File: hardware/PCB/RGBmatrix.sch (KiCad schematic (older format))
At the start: 41 parts

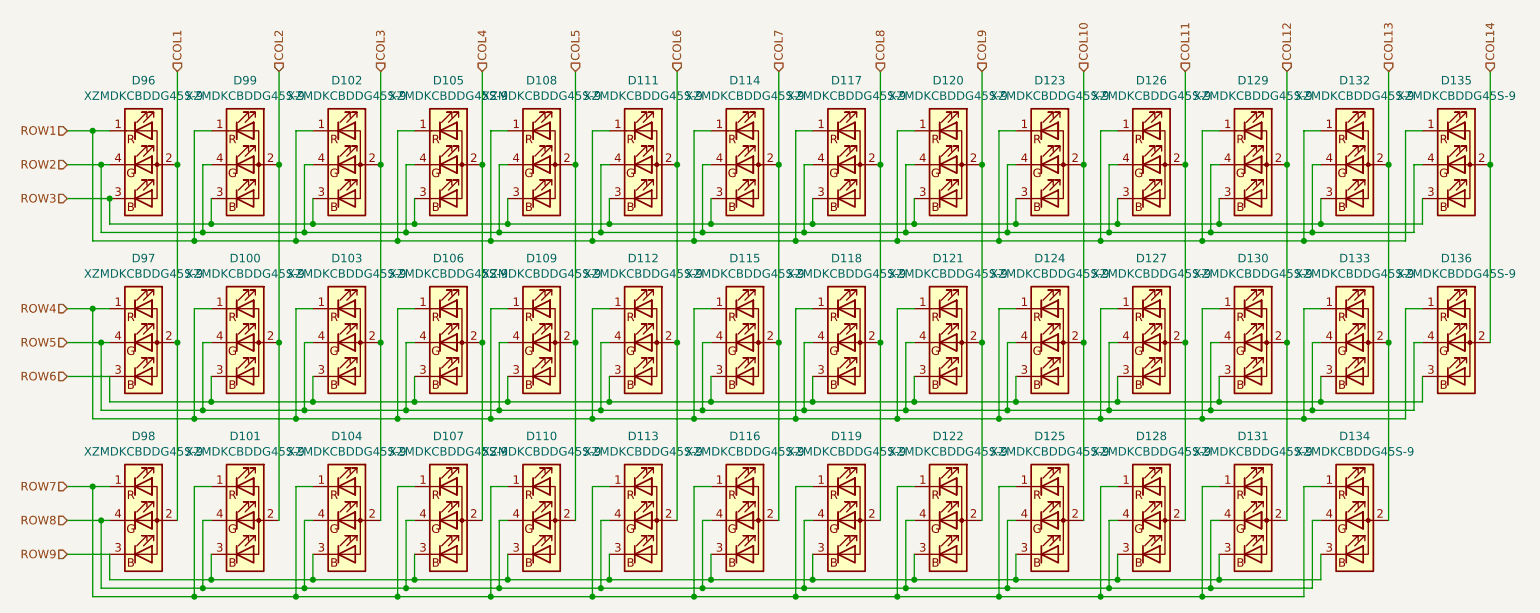
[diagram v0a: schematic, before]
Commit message: update render, remove useless files, fix the decoupeling
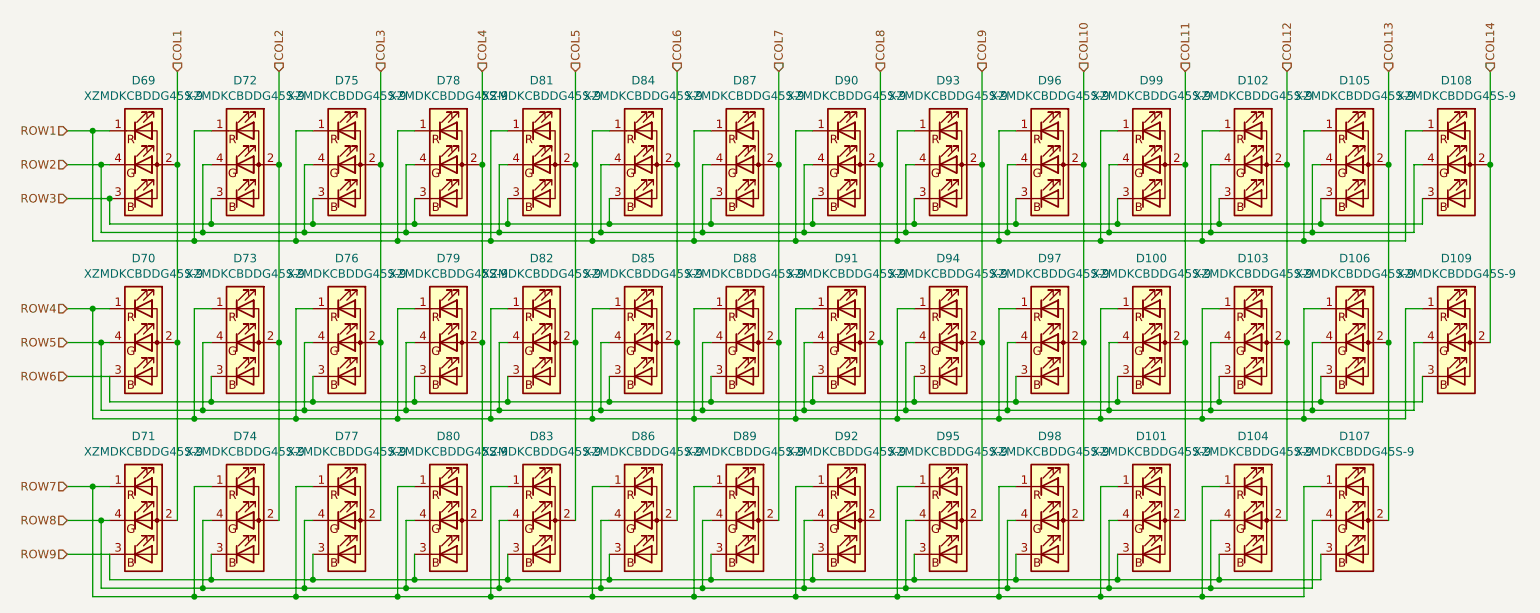
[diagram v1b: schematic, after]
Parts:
- renumbered D127 to D100, D128 to D101, D129 to D102, D130 to D103, D131 to D104, D132 to D105, D133 to D106, D134 to D107, D135 to D108, D136 to D109, D96 to D69, D97 to D70, D98 to D71, D99 to D72, D100 to D73, D101 to D74, D102 to D75, D103 to D76, D104 to D77, D105 to D78, D106 to D79, D107 to D80, D108 to D81, D109 to D82, D110 to D83, D111 to D84, D112 to D85, D113 to D86, D114 to D87, D115 to D88, D116 to D89, D117 to D90, D118 to D91, D119 to D92, D120 to D93, D121 to D94, D122 to D95, D123 to D96, D124 to D97, D125 to D98, D126 to D99

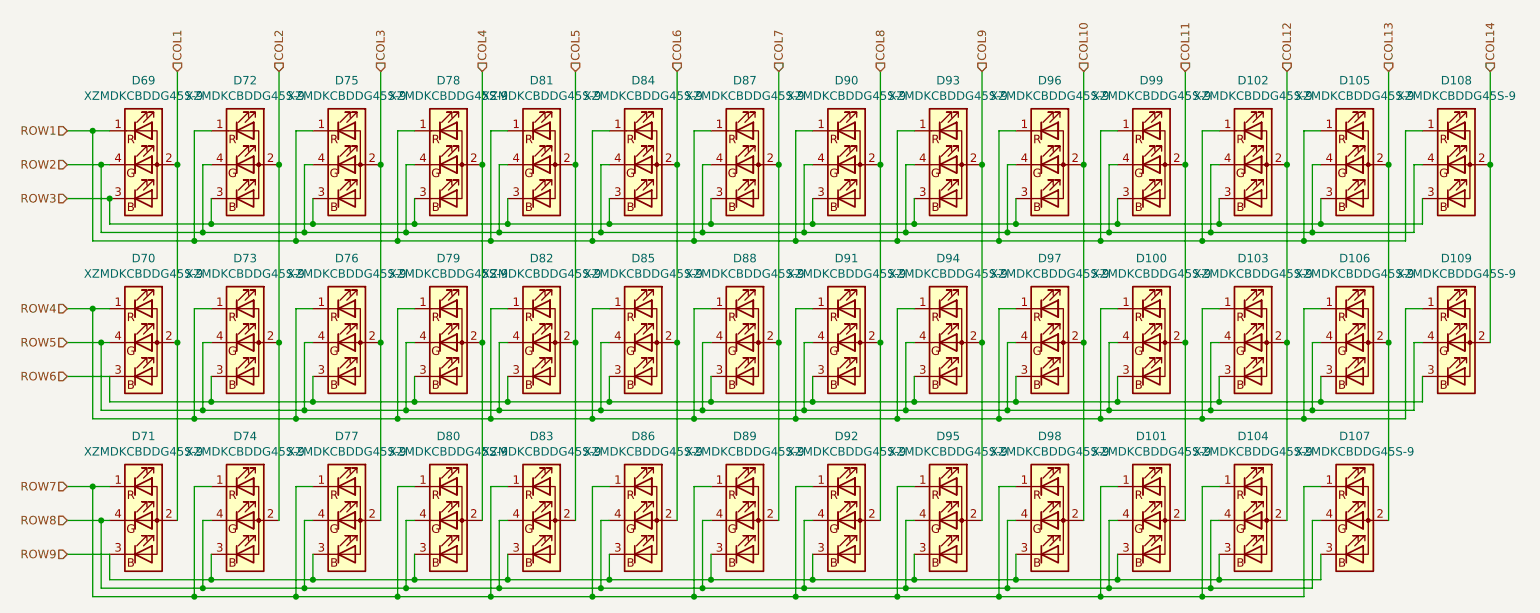
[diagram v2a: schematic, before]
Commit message: Make sure GPL done correctly, rev0.2 ready, not going to make it either
Need to make it nicer
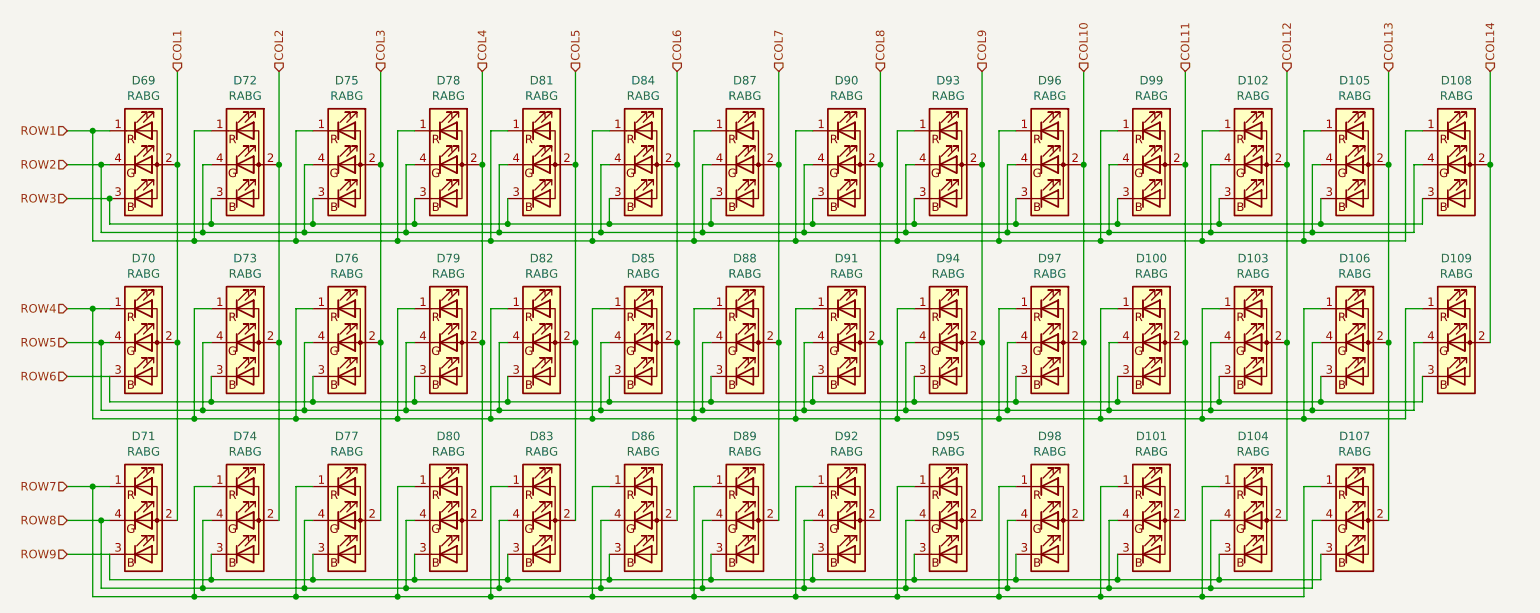
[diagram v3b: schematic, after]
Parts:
- D100, D101, D102, D103, D104, D105, D106, D107, D108, D109, D69, D70, D71, D72, D73, D74, D75, D76, D77, D78, D79, D80, D81, D82, D83, D84, D85, D86, D87, D88, D89, D90, D91, D92, D93, D94, D95, D96, D97, D98, D99: value XZMDKCBDDG45S-9 -> RABG

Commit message: Rev 0.5
1. Use a better 1205 LED (much chaper on LCSC)
2. Fix the crystal CL, Rext
3. did a better job on wiring (but might come with power issues?)
4. fix the key position (0.01mm shifted so its a big fix)
5. generate better bom files
6. add in LCSC and part number so easier to source
0.4 is gone
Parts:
- D100, D101, D102, D103, D104, D105, D106, D107, D108, D109, D69, D70, D71, D72, D73, D74, D75, D76, D77, D78, D79, D80, D81, D82, D83, D84, D85, D86, D87, D88, D89, D90, D91, D92, D93, D94, D95, D96, D97, D98, D99: footprint KiCad:XZMDKCBDDG45S9_fixed -> KiCad:RGB_LED_1205; LCSC (none) -> C409782; Part Number XZMDKCBDDG45S-9 -> MHT150RGBCT

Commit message: Remove some unused
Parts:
- D100, D101, D102, D103, D104, D105, D106, D107, D108, D109, D69, D70, D71, D72, D73, D74, D75, D76, D77, D78, D79, D80, D81, D82, D83, D84, D85, D86, D87, D88, D89, D90, D91, D92, D93, D94, D95, D96, D97, D98, D99: footprint KiCad:RGB_LED_1205 -> KiCad:RGB_LED_1204_reverse
